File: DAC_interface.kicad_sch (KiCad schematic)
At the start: 10 parts, among them IC2 ES9038Q2M, Y2 SiT8209AI-21-33S-100.000000X

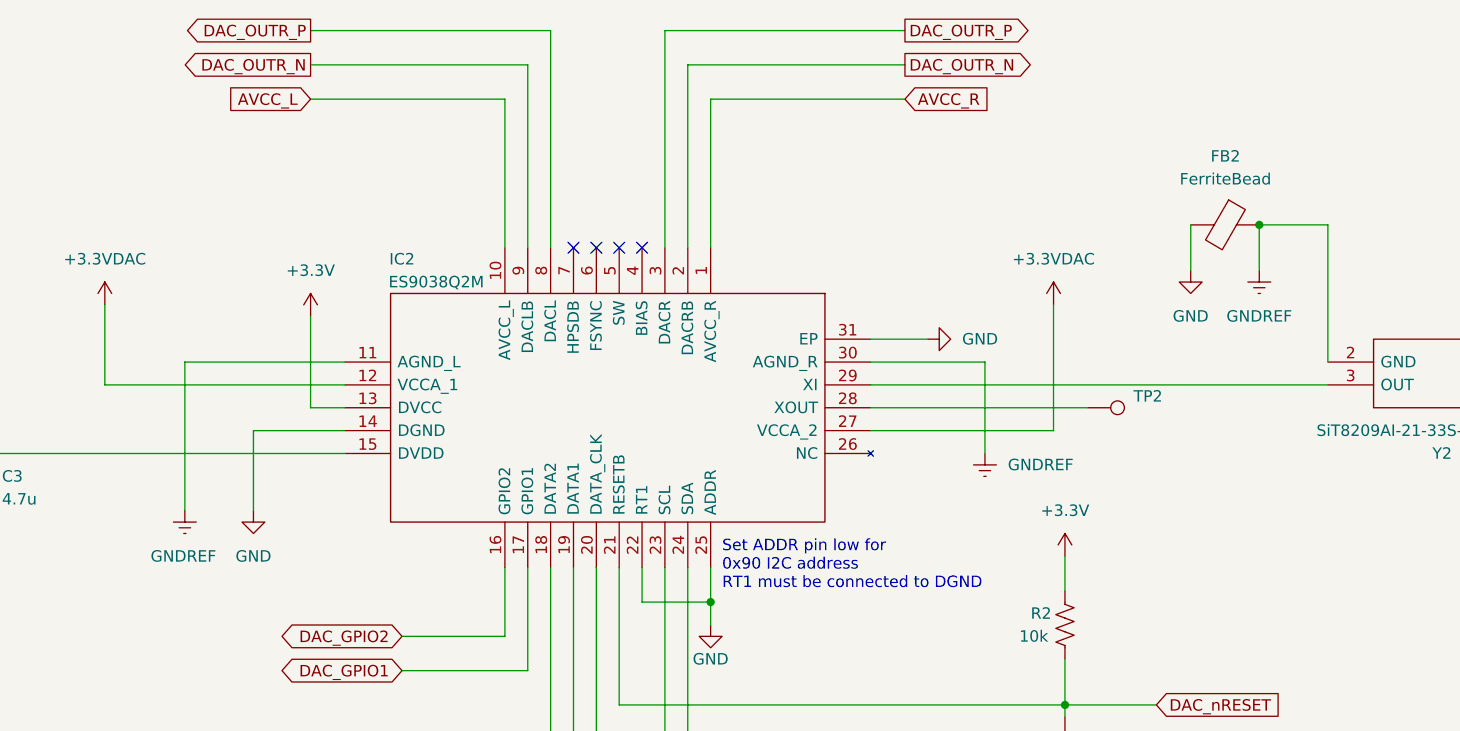
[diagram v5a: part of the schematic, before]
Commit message: Adding footprints. WIP PCB, finished routing, no ground planes yet
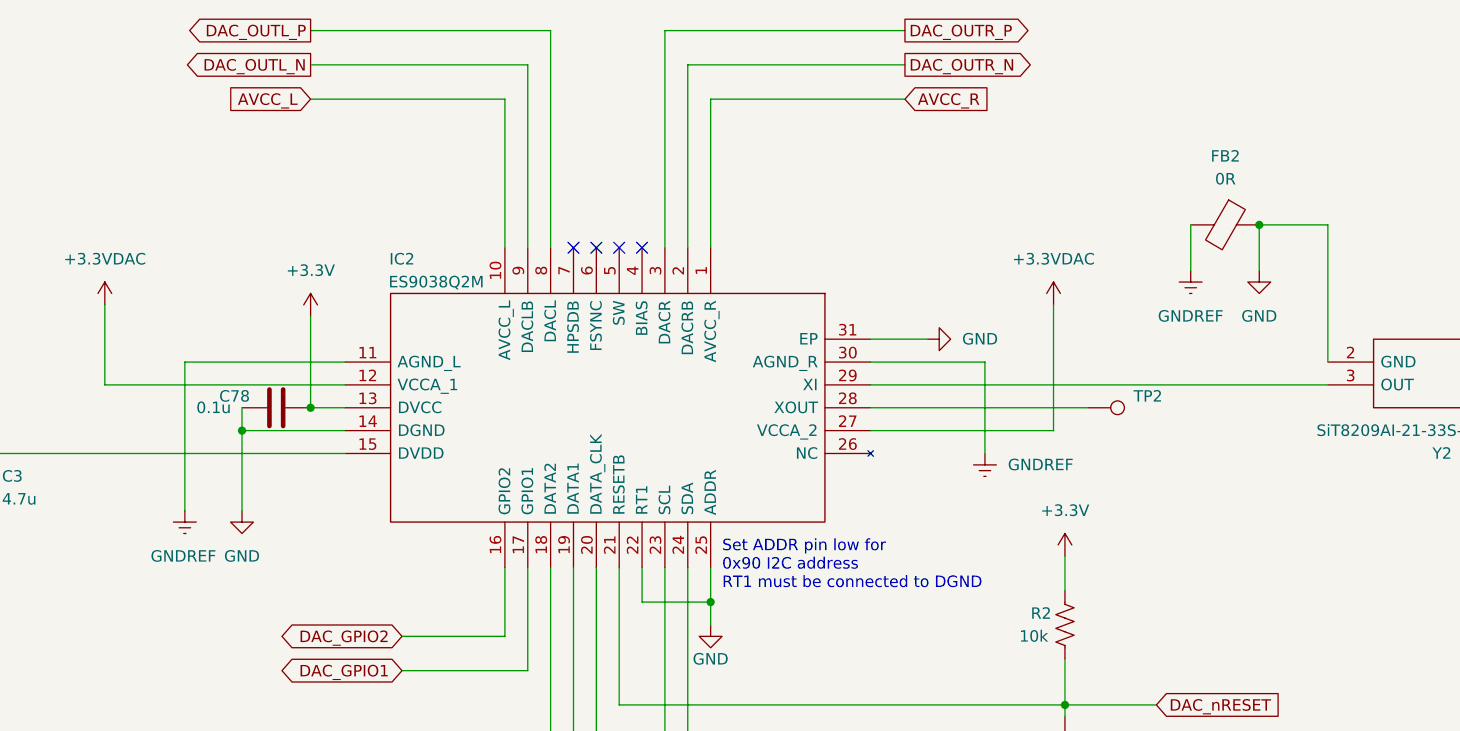
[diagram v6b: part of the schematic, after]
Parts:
- added C78: 0.1u, Capacitor_SMD:C_0805_2012Metric_Pad1.18x1.45mm_HandSolder, symbol Device:C
- FB2: value FerriteBead -> 0R; footprint (none) -> SamacSys_Parts:BEADC2012X110N
- TP2: footprint TestPoint:TestPoint_Pad_D2.0mm -> TestPoint:TestPoint_Pad_D1.0mm
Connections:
- net +3V3: now also C78.1
- net DAC_OUTR_N: no longer IC2.9 (DACLB)
- net DAC_OUTR_P: no longer IC2.8 (DACL)
- net GND: now also FB2.1, Y2.2 (GND), C78.2; no longer FB2.2
- net GNDREF: now also FB2.2; no longer FB2.1, Y2.2 (GND)
- new net DAC_OUTL_N: IC2.9 (DACLB)
- new net DAC_OUTL_P: IC2.8 (DACL)
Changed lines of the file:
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@@
   (junction (at 181.61 113.03) (diameter 0) (color 0 0 0 0)
+  )
+  (junction (at 90.17 82.55) (diameter 0) (color 0 0 0 0)
+  )
+  (junction (at 97.79 80.01) (diameter 0) (color 0 0 0 0)
   )
   (junction (at 246.38 59.69) (diameter 0) (color 0 0 0 0)
@@
     (stroke (width 0) (type default) (color 0 0 0 0))
   )
+  (wire (pts (xy 52.07 92.71) (xy 55.88 92.71))
+    (stroke (width 0) (type default) (color 0 0 0 0))
+  )
+  (wire (pts (xy 210.82 59.69) (xy 203.2 59.69))
+    (stroke (width 0) (type default) (color 0 0 0 0))
+  )
+  (wire (pts (xy 142.24 97.79) (xy 142.24 101.6))
+    (stroke (width 0) (type default) (color 0 0 0 0))
+  )
   (wire (pts (xy 195.58 59.69) (xy 195.58 64.77))
     (stroke (width 0) (type default) (color 0 0 0 0))
   )
-  (wire (pts (xy 52.07 92.71) (xy 55.88 92.71))
-    (stroke (width 0) (type default) (color 0 0 0 0))
-  )
-  (wire (pts (xy 210.82 59.69) (xy 203.2 59.69))
-    (stroke (width 0) (type default) (color 0 0 0 0))
-  )
-  (wire (pts (xy 142.24 97.79) (xy 142.24 101.6))
-    (stroke (width 0) (type default) (color 0 0 0 0))
-  )
   (wire (pts (xy 139.7 97.79) (xy 139.7 135.89))
     (stroke (width 0) (type default) (color 0 0 0 0))
@@
     (stroke (width 0) (type default) (color 0 0 0 0))
   )
-  (wire (pts (xy 91.44 82.55) (xy 91.44 91.44))
+  (wire (pts (xy 90.17 82.55) (xy 90.17 91.44))
     (stroke (width 0) (type default) (color 0 0 0 0))
   )
@@
     (stroke (width 0) (type default) (color 0 0 0 0))
   )
+  (wire (pts (xy 203.2 59.69) (xy 203.2 64.77))
+    (stroke (width 0) (type default) (color 0 0 0 0))
+  )
   (wire (pts (xy 83.82 74.93) (xy 83.82 91.44))
     (stroke (width 0) (type default) (color 0 0 0 0))
@@
     (stroke (width 0) (type default) (color 0 0 0 0))
   )
-  (wire (pts (xy 203.2 59.69) (xy 203.2 64.77))
-    (stroke (width 0) (type default) (color 0 0 0 0))
-  )
   (wire (pts (xy 129.54 97.79) (xy 129.54 144.78))
     (stroke (width 0) (type default) (color 0 0 0 0))
@@
     (stroke (width 0) (type default) (color 0 0 0 0))
   )
+  (wire (pts (xy 90.17 80.01) (xy 90.17 82.55))
+    (stroke (width 0) (type default) (color 0 0 0 0))
+  )
   (wire (pts (xy 101.6 77.47) (xy 74.93 77.47))
     (stroke (width 0) (type default) (color 0 0 0 0))
@@
     (stroke (width 0) (type default) (color 0 0 0 0))
   )
-  (wire (pts (xy 101.6 82.55) (xy 91.44 82.55))
+  (wire (pts (xy 101.6 82.55) (xy 90.17 82.55))
     (stroke (width 0) (type default) (color 0 0 0 0))
   )
@@
     )
   )
-  (global_label "DAC_OUTR_N" (shape output) (at 97.79 41.91 180) (fields_autoplaced)
+  (global_label "DAC_OUTL_N" (shape output) (at 97.79 41.91 180) (fields_autoplaced)
     (effects (font (size 1.27 1.27)) (justify right))
-    (property "Intersheet References" "${INTERSHEET_REFS}" (id 0) (at 83.584 41.9894 0)
+    (property "Intersheet References" "${INTERSHEET_REFS}" (id 0) (at 83.8259 41.8306 0)
       (effects (font (size 1.27 1.27)) (justify right) hide)
     )
   )
-  (global_label "DAC_OUTR_P" (shape output) (at 97.79 38.1 180) (fields_autoplaced)
+  (global_label "DAC_OUTL_P" (shape output) (at 97.79 38.1 180) (fields_autoplaced)
     (effects (font (size 1.27 1.27)) (justify right))
-    (property "Intersheet References" "${INTERSHEET_REFS}" (id 0) (at 83.6445 38.1794 0)
+    (property "Intersheet References" "${INTERSHEET_REFS}" (id 0) (at 83.8864 38.0206 0)
       (effects (font (size 1.27 1.27)) (justify right) hide)
     )
@@
     (pin "4")
   )
-  (symbol (lib_id "power:GND") (at 195.58 64.77 0) (unit 1)
-    (in_bom yes) (on_board yes) (fields_autoplaced)
-    (property "Reference" "#PWR0115" (id 0) (at 195.58 71.12 0)
-      (effects (font (size 1.27 1.27)) hide)
-    )
-    (property "Value" "GND" (id 1) (at 195.58 69.85 0))
-    (property "Footprint" "" (id 2) (at 195.58 64.77 0)
-      (effects (font (size 1.27 1.27)) hide)
-    )
-    (property "Datasheet" "" (id 3) (at 195.58 64.77 0)
+  (symbol (lib_id "power:GND") (at 203.2 64.77 0) (unit 1)
+    (in_bom yes) (on_board yes) (fields_autoplaced)
+    (property "Reference" "#PWR0115" (id 0) (at 203.2 71.12 0)
+      (effects (font (size 1.27 1.27)) hide)
+    )
+    (property "Value" "GND" (id 1) (at 203.2 69.85 0))
+    (property "Footprint" "" (id 2) (at 203.2 64.77 0)
+      (effects (font (size 1.27 1.27)) hide)
+    )
+    (property "Datasheet" "" (id 3) (at 203.2 64.77 0)
       (effects (font (size 1.27 1.27)) hide)
     )
@@
     (pin "1")
   )
-  (symbol (lib_id "power:GND") (at 91.44 91.44 0) (unit 1)
-    (in_bom yes) (on_board yes) (fields_autoplaced)
-    (property "Reference" "#PWR0108" (id 0) (at 91.44 97.79 0)
-      (effects (font (size 1.27 1.27)) hide)
-    )
-    (property "Value" "GND" (id 1) (at 91.44 96.52 0))
-    (property "Footprint" "" (id 2) (at 91.44 91.44 0)
-      (effects (font (size 1.27 1.27)) hide)
-    )
-    (property "Datasheet" "" (id 3) (at 91.44 91.44 0)
+  (symbol (lib_id "power:GND") (at 90.17 91.44 0) (unit 1)
+    (in_bom yes) (on_board yes) (fields_autoplaced)
+    (property "Reference" "#PWR0108" (id 0) (at 90.17 97.79 0)
+      (effects (font (size 1.27 1.27)) hide)
+    )
+    (property "Value" "GND" (id 1) (at 90.17 96.52 0))
+    (property "Footprint" "" (id 2) (at 90.17 91.44 0)
+      (effects (font (size 1.27 1.27)) hide)
+    )
+    (property "Datasheet" "" (id 3) (at 90.17 91.44 0)
       (effects (font (size 1.27 1.27)) hide)
     )
@@
     (pin "1")
   )
-  (symbol (lib_id "power:GNDREF") (at 203.2 64.77 0) (unit 1)
-    (in_bom yes) (on_board yes) (fields_autoplaced)
-    (property "Reference" "#PWR0114" (id 0) (at 203.2 71.12 0)
-      (effects (font (size 1.27 1.27)) hide)
-    )
-    (property "Value" "GNDREF" (id 1) (at 203.2 69.85 0))
-    (property "Footprint" "" (id 2) (at 203.2 64.77 0)
-      (effects (font (size 1.27 1.27)) hide)
-    )
-    (property "Datasheet" "" (id 3) (at 203.2 64.77 0)
+  (symbol (lib_id "power:GNDREF") (at 195.58 64.77 0) (unit 1)
+    (in_bom yes) (on_board yes) (fields_autoplaced)
+    (property "Reference" "#PWR0114" (id 0) (at 195.58 71.12 0)
+      (effects (font (size 1.27 1.27)) hide)
+    )
+    (property "Value" "GNDREF" (id 1) (at 195.58 69.85 0))
+    (property "Footprint" "" (id 2) (at 195.58 64.77 0)
+      (effects (font (size 1.27 1.27)) hide)
+    )
+    (property "Datasheet" "" (id 3) (at 195.58 64.77 0)
       (effects (font (size 1.27 1.27)) hide)
     )
@@
       (effects (font (size 1.27 1.27)) (justify left) hide)
     )
-    (property "Footprint" "TestPoint:TestPoint_Pad_D2.0mm" (id 2) (at 184.15 85.09 0)
+    (property "Footprint" "TestPoint:TestPoint_Pad_D1.0mm" (id 2) (at 184.15 85.09 0)
       (effects (font (size 1.27 1.27)) hide)
     )
@@
     (in_bom yes) (on_board yes) (fields_autoplaced)
     (property "Reference" "FB2" (id 0) (at 199.4408 52.07 90))
-    (property "Value" "FerriteBead" (id 1) (at 199.4408 54.61 90))
-    (property "Footprint" "" (id 2) (at 199.39 57.912 90)
+    (property "Value" "0R" (id 1) (at 199.4408 54.61 90))
+    (property "Footprint" "SamacSys_Parts:BEADC2012X110N" (id 2) (at 199.39 57.912 90)
       (effects (font (size 1.27 1.27)) hide)
     )
@@
     (pin "9")
   )
+  (symbol (lib_id "Device:C") (at 93.98 80.01 270) (unit 1)
+    (in_bom yes) (on_board yes)
+    (property "Reference" "C78" (id 0) (at 87.63 78.74 90)
+      (effects (font (size 1.27 1.27)) (justify left))
+    )
+    (property "Value" "0.1u" (id 1) (at 85.09 80.01 90)
+      (effects (font (size 1.27 1.27)) (justify left))
+    )
+    (property "Footprint" "Capacitor_SMD:C_0805_2012Metric_Pad1.18x1.45mm_HandSolder" (id 2) (at 90.17 80.9752 0)
+      (effects (font (size 1.27 1.27)) hide)
+    )
+    (property "Datasheet" "~" (id 3) (at 93.98 80.01 0)
+      (effects (font (size 1.27 1.27)) hide)
+    )
+    (pin "1")
+    (pin "2")
+  )
   (symbol (lib_id "Device:R_US") (at 236.22 67.31 0) (unit 1)

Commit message: Adding part numbers for passives
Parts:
- C2, C5: Mouser Part Number (none) -> 581-0805YC224JAT2A; Part Number (none) -> 0805YC224JAT2A
- C3: Mouser Part Number (none) -> 963-LMK212ABJ475KG8T; Part Number (none) -> LMK212ABJ475KG8T
- C4: Mouser Part Number (none) -> 581-0805ZD225KAT4A; Part Number (none) -> 0805ZD225KAT4A
- C78: Mouser Part Number (none) -> 187-CL21B104KBCNFNC; Part Number (none) -> CL21B104KBCNFNC
- FB2: Mouser Part Number (none) -> 704-MFBW1V2012-000-R; Part Number (none) -> MFBW1V2012-000-R
- R2: Mouser Part Number (none) -> 80-C0805C202F4HAUTO; Part Number (none) -> C0805C202F4HACAUTO
- R3: Mouser Part Number (none) -> 667-ERJ-HP6D1001V; Part Number (none) -> ERJ-HP6D1001V
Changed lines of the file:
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@@
+      (effects (font (size 1.27 1.27)) hide)
+    )
+    (property "Part Number" "0805ZD225KAT4A" (id 4) (at 181.61 118.11 0)
+      (effects (font (size 1.27 1.27)) hide)
+    )
+    (property "Mouser Part Number" "581-0805ZD225KAT4A" (id 5) (at 181.61 118.11 0)
       (effects (font (size 1.27 1.27)) hide)
     )
@@
       (effects (font (size 1.27 1.27)) hide)
     )
+    (property "Part Number" "C0805C202F4HACAUTO" (id 4) (at 181.61 104.14 0)
+      (effects (font (size 1.27 1.27)) hide)
+    )
+    (property "Mouser Part Number" "80-C0805C202F4HAUTO" (id 5) (at 181.61 104.14 0)
+      (effects (font (size 1.27 1.27)) hide)
+    )
     (pin "1")
     (pin "2")
@@
       (effects (font (size 1.27 1.27)) hide)
     )
+    (property "Part Number" "0805YC224JAT2A" (id 4) (at 246.38 81.28 0)
+      (effects (font (size 1.27 1.27)) hide)
+    )
+    (property "Mouser Part Number" "581-0805YC224JAT2A" (id 5) (at 246.38 81.28 0)
+      (effects (font (size 1.27 1.27)) hide)
+    )
     (pin "1")
     (pin "2")
@@
     )
     (property "Datasheet" "~" (id 3) (at 52.07 88.9 0)
+      (effects (font (size 1.27 1.27)) hide)
+    )
+    (property "Part Number" "0805YC224JAT2A" (id 4) (at 52.07 88.9 0)
+      (effects (font (size 1.27 1.27)) hide)
+    )
+    (property "Mouser Part Number" "581-0805YC224JAT2A" (id 5) (at 52.07 88.9 0)
       (effects (font (size 1.27 1.27)) hide)
     )
@@
       (effects (font (size 1.27 1.27)) hide)
     )
+    (property "Part Number" "MFBW1V2012-000-R" (id 4) (at 199.39 59.69 90)
+      (effects (font (size 1.27 1.27)) hide)
+    )
+    (property "Mouser Part Number" "704-MFBW1V2012-000-R" (id 5) (at 199.39 59.69 90)
+      (effects (font (size 1.27 1.27)) hide)
+    )
     (pin "1")
     (pin "2")
@@
     )
     (property "Datasheet" "~" (id 3) (at 59.69 88.9 0)
+      (effects (font (size 1.27 1.27)) hide)
+    )
+    (property "Part Number" "LMK212ABJ475KG8T" (id 4) (at 59.69 88.9 0)
+      (effects (font (size 1.27 1.27)) hide)
+    )
+    (property "Mouser Part Number" "963-LMK212ABJ475KG8T" (id 5) (at 59.69 88.9 0)
       (effects (font (size 1.27 1.27)) hide)
     )
@@
       (effects (font (size 1.27 1.27)) hide)
     )
+    (property "Part Number" "CL21B104KBCNFNC" (id 4) (at 93.98 80.01 90)
+      (effects (font (size 1.27 1.27)) hide)
+    )
+    (property "Mouser Part Number" "187-CL21B104KBCNFNC" (id 5) (at 93.98 80.01 90)
+      (effects (font (size 1.27 1.27)) hide)
+    )
     (pin "1")
     (pin "2")
@@
       (effects (font (size 1.27 1.27)) hide)
     )
+    (property "Part Number" "ERJ-HP6D1001V" (id 4) (at 236.22 67.31 0)
+      (effects (font (size 1.27 1.27)) hide)
+    )
+    (property "Mouser Part Number" "667-ERJ-HP6D1001V" (id 5) (at 236.22 67.31 0)
+      (effects (font (size 1.27 1.27)) hide)
+    )

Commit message: Adding more part numbers. WIP verifying part numbers
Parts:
- C3: Mouser Part Number 963-LMK212ABJ475KG8T -> 80-C0805C104K8RAUTO; Part Number LMK212ABJ475KG8T -> C0805C104K8RACAUTO
- R2: Mouser Part Number 80-C0805C202F4HAUTO -> 603-RT0805BRD0710KL; Part Number C0805C202F4HACAUTO -> RT0805BRD0710KL
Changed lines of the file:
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@@
       (effects (font (size 1.27 1.27)) hide)
     )
-    (property "Part Number" "C0805C202F4HACAUTO" (id 4) (at 181.61 104.14 0)
-      (effects (font (size 1.27 1.27)) hide)
-    )
-    (property "Mouser Part Number" "80-C0805C202F4HAUTO" (id 5) (at 181.61 104.14 0)
+    (property "Part Number" "RT0805BRD0710KL" (id 4) (at 181.61 104.14 0)
+      (effects (font (size 1.27 1.27)) hide)
+    )
+    (property "Mouser Part Number" "603-RT0805BRD0710KL" (id 5) (at 181.61 104.14 0)
       (effects (font (size 1.27 1.27)) hide)
     )
@@
       (effects (font (size 1.27 1.27)) hide)
     )
-    (property "Part Number" "LMK212ABJ475KG8T" (id 4) (at 59.69 88.9 0)
-      (effects (font (size 1.27 1.27)) hide)
-    )
-    (property "Mouser Part Number" "963-LMK212ABJ475KG8T" (id 5) (at 59.69 88.9 0)
-      (effects (font (size 1.27 1.27)) hide)
-    )
+    (property "Part Number" "C0805C104K8RACAUTO" (id 4) (at 59.69 88.9 0)
+      (effects (font (size 1.27 1.27)) hide)
+    )
+    (property "Mouser Part Number" "80-C0805C104K8RAUTO" (id 5) (at 59.69 88.9 0)
+      (effects (font (size 1.27 1.27)) hide)
+    )
